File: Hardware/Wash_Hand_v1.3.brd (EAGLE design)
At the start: 71.1 x 48.3 mm, 65 parts, among them IC1 LM358D, IC2 LP298XS, IC3 4050D, J1 I2C, J2 ICSP, J3 SPI, J5 EXT_VCC, J6 6_PIN_SERIAL_CABLEPTH, Q1 16.0 Mhz, U1 328P

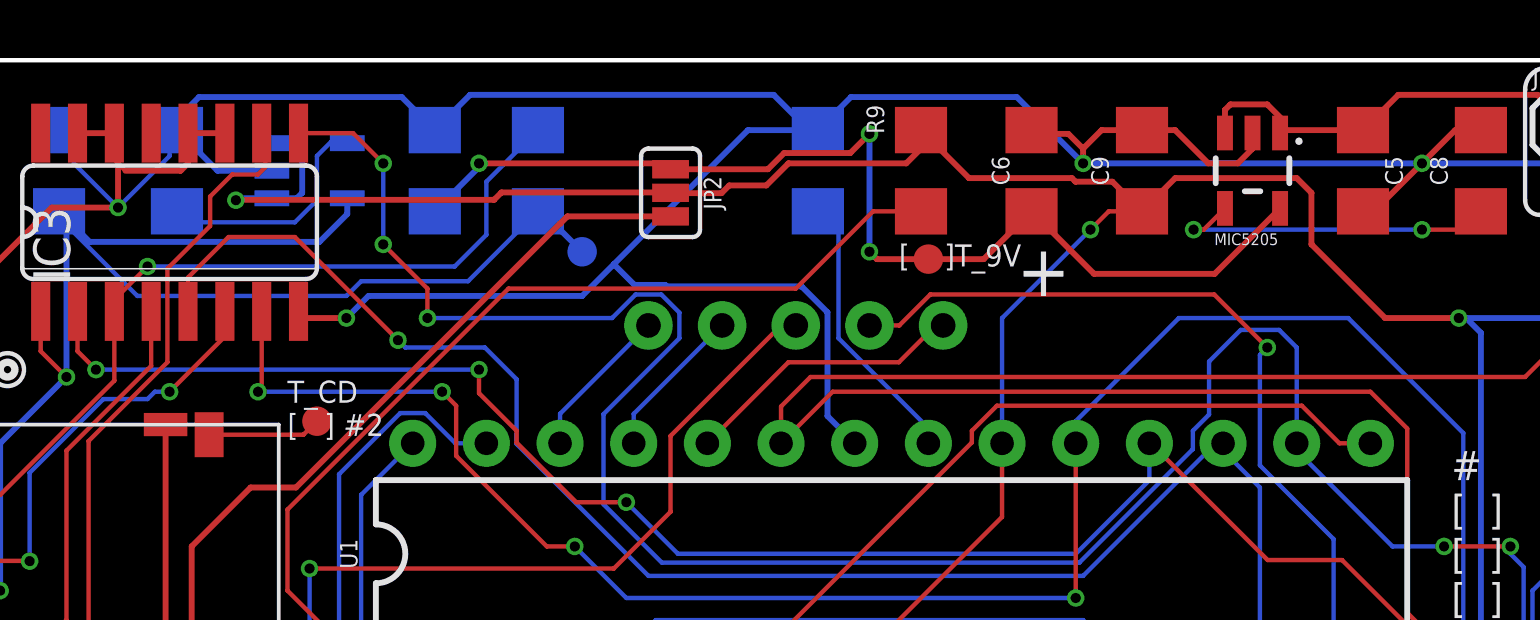
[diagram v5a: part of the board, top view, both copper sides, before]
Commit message: Board: Swap C7 with C9.
The LP298 has C9,C10,C11 but in the board right next to it are:
_C7_,C10,C11!

The MIC5205 has C5,C6,C7,C8 but in the board right next to it
are: C5,C6,_C9_, and C8.

Lets swap them around to be closer to their own circuits.

Signed-off-by: Konrad Rzeszutek Wilk <konrad@kernel.org>
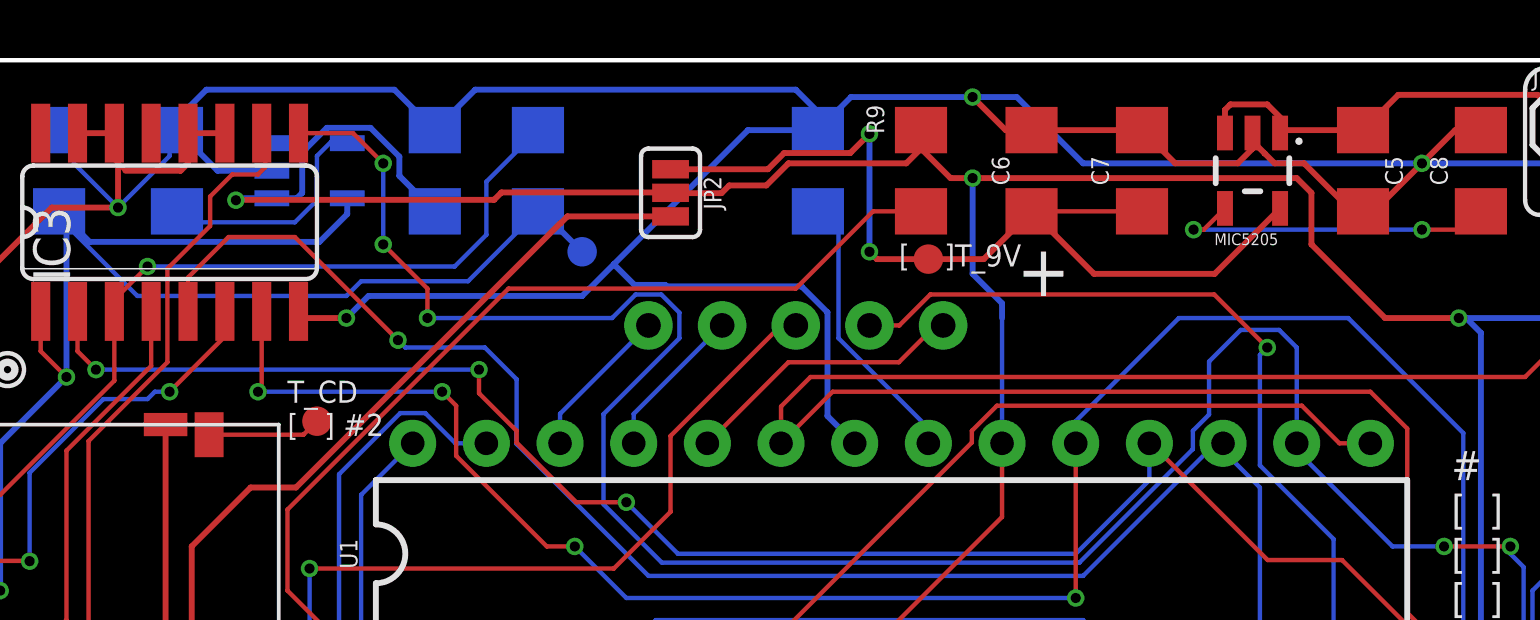
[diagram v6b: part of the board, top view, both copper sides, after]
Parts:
- moved C7 24.4 mm to (45.5, 44.5), flipped to the top
- moved C9 24.4 mm to (21.1, 44.5), flipped to the bottom
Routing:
- net 0: track 348.8 -> 355.7 mm
- net N$10: track 37.2 -> 32.0 mm, vias 3 -> 2
- net VCC: track 191.5 -> 195.7 mm

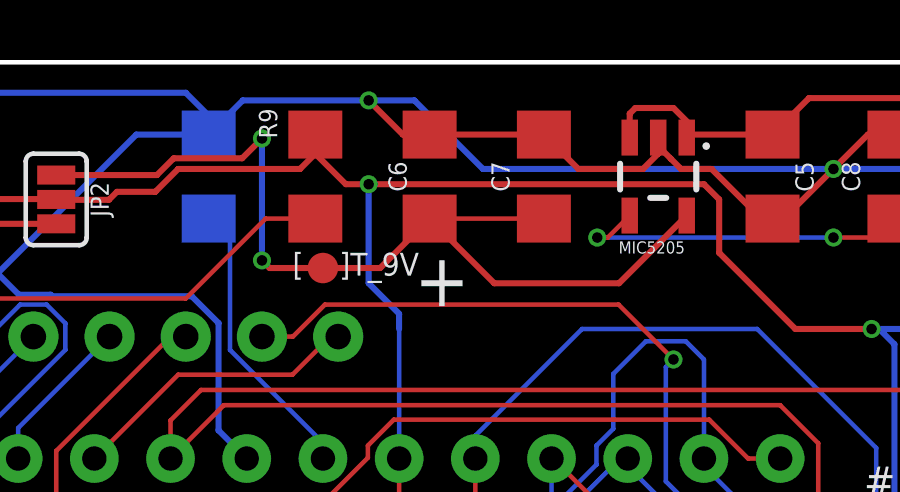
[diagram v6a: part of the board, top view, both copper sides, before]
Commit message: Board/Schematic: Swap names (and values)of C6 and C7
They are right next to each other - and we want
the 1uF to be closer to MIC5205.

It was easier to swap the names than moving
the SMD on the board.

Signed-off-by: Konrad Rzeszutek Wilk <konrad@kernel.org>
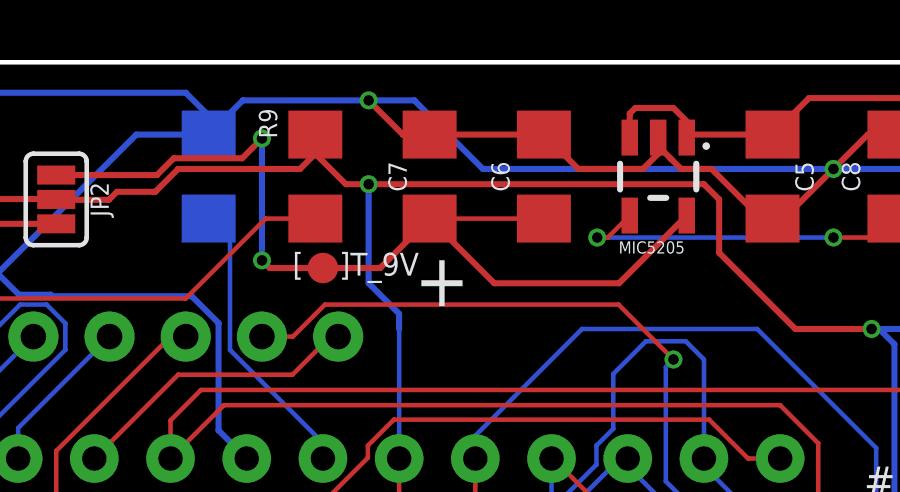
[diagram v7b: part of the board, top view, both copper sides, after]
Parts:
- C6: value 2.2uF -> 2.2uF T
- moved C6 3.81 mm to (45.5, 44.5)
- moved C7 3.81 mm to (41.7, 44.5)
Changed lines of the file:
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@@
 <attribute name="VALUE" value="1.0uF" x="52.324" y="44.45" size="0.6096" layer="27" font="vector" ratio="20" rot="R270" align="top-center"/>
 </element>
-<element name="C6" library="SparkFun-Capacitors" library_urn="urn:adsk.eagle:library:510" package="1206" package3d_urn="urn:adsk.eagle:package:37426/1" value="2.2uF" x="41.656" y="44.45" smashed="yes" rot="R90">
+<element name="C7" library="SparkFun-Capacitors" library_urn="urn:adsk.eagle:library:510" package="1206" package3d_urn="urn:adsk.eagle:package:37426/1" value="1uF" x="41.656" y="44.45" smashed="yes" rot="R90">
 <attribute name="NAME" x="40.894" y="44.45" size="0.6096" layer="25" font="vector" ratio="20" rot="R90" align="bottom-center"/>
 <attribute name="PROD_ID" value="CAP-09822" x="41.656" y="44.45" size="1.778" layer="27" rot="R90" display="off"/>
 <attribute name="VALUE" value="1.0uF" x="42.418" y="44.45" size="0.6096" layer="27" font="vector" ratio="20" rot="R90" align="top-center"/>
 </element>
-<element name="C7" library="SparkFun-Capacitors" library_urn="urn:adsk.eagle:library:510" package="1206" package3d_urn="urn:adsk.eagle:package:37426/1" value="1uF" x="45.466" y="44.45" smashed="yes" rot="R90">
+<element name="C6" library="SparkFun-Capacitors" library_urn="urn:adsk.eagle:library:510" package="1206" package3d_urn="urn:adsk.eagle:package:37426/1" value="2.2uF T" x="45.466" y="44.45" smashed="yes" rot="R90">
 <attribute name="NAME" x="44.323" y="44.45" size="0.6096" layer="25" font="vector" ratio="20" rot="R90" align="bottom-center"/>
 <attribute name="PROD_ID" value="CAP-09822" x="45.466" y="44.45" size="1.778" layer="27" rot="R90" display="off"/>
@@
 <contactref element="J6" pad="GND"/>
 <contactref element="MIC5205" pad="2"/>
+<contactref element="C7" pad="2"/>
 <contactref element="C6" pad="2"/>
-<contactref element="C7" pad="2"/>
 <contactref element="J4" pad="2"/>
 <contactref element="TM1" pad="1"/>
@@
 <signal name="N$10">
 <contactref element="MIC5205" pad="5"/>
+<contactref element="C7" pad="1"/>
 <contactref element="C6" pad="1"/>
-<contactref element="C7" pad="1"/>
 <contactref element="JP2" pad="1"/>
 <contactref element="TP5" pad="P$1"/>

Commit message: Release: v1.3a.3
Signed-off-by: Konrad Rzeszutek Wilk <konrad@kernel.org>
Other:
- board text added: "v1.3a.3"
- board text removed: "v1.3a.2"
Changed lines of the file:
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@@
 <circle x="6.35" y="37.592" radius="0.254" width="0.254" layer="25"/>
 <circle x="6.35" y="37.592" radius="0.567959375" width="0.1524" layer="25"/>
-<text x="21.336" y="19.558" size="1.778" layer="26" ratio="14" rot="MR0">v1.3a.2</text>
+<text x="21.336" y="19.558" size="1.778" layer="26" ratio="14" rot="MR0">v1.3a.3</text>
 <text x="56.134" y="15.494" size="1.016" layer="25" ratio="14">#
 [  ]
@@
 <element name="MICROSD" library="darnok_microsd" package="114-00841-68" value="114-00841-68" x="9.94" y="29.718" smashed="yes" rot="R270"/>
 <element name="FRAME1" library="darnok_frame" package="REVISION_TEXT" value="" x="54.356" y="22.606" smashed="yes">
-<attribute name="REVISION" value="v1.3a.2" x="54.356" y="22.606" size="1.778" layer="27" display="off"/>
+<attribute name="REVISION" value="v1.3a.3" x="54.356" y="22.606" size="1.778" layer="27" display="off"/>
 </element>
 <element name="FRAME2" library="darnok_frame" package="REVISION_TEXT" value="" x="18.542" y="19.812" smashed="yes" rot="MR0">
-<attribute name="REVISION" value="v1.3a.2" x="18.542" y="19.812" size="1.778" layer="28" rot="MR0" display="off"/>
+<attribute name="REVISION" value="v1.3a.3" x="18.542" y="19.812" size="1.778" layer="28" rot="MR0" display="off"/>
 </element>
 <element name="R12" library="darnok_common" package="1206" value="1K" x="16.764" y="10.922" smashed="yes" rot="MR90">
